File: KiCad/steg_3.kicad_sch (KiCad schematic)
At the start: 26 parts, among them U13 W65C02S

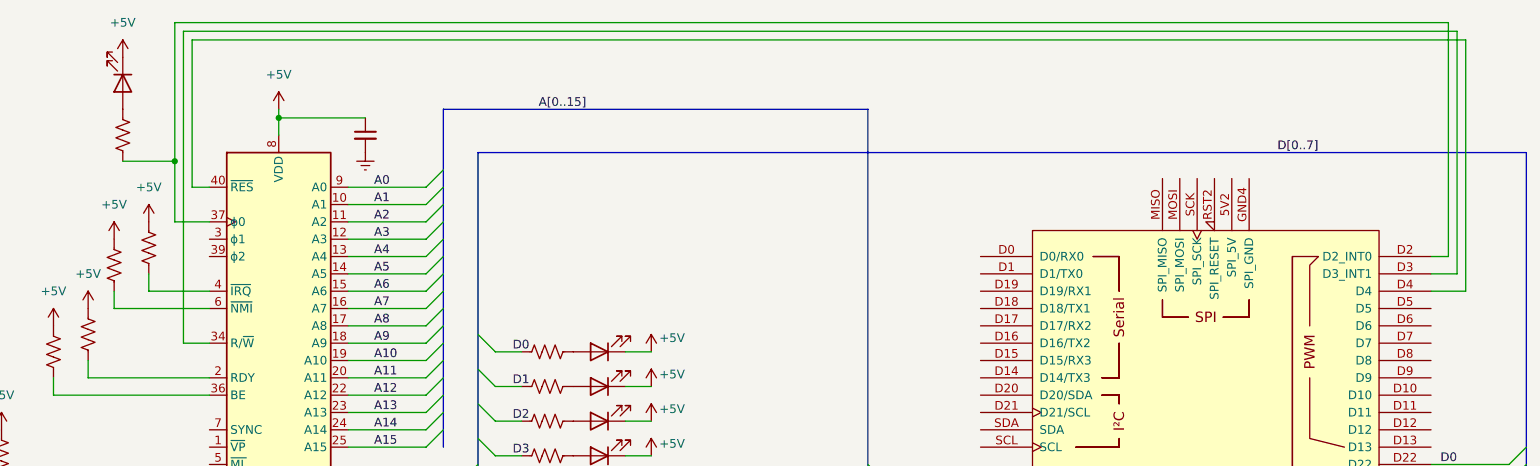
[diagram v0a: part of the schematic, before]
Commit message: Revert "Add trim potentiometer symbol and update power symbols in schematics"
This reverts commit c4bb345892a428583a00d61d4c040ffcc3a1eb40.
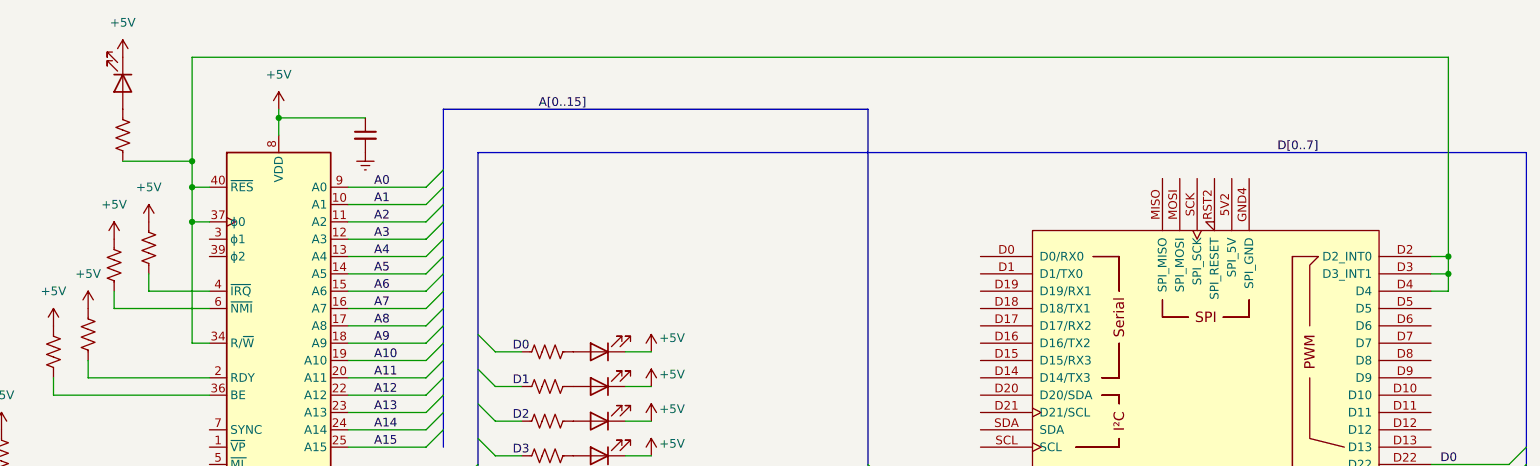
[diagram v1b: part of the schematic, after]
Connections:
- net at A7.D3 (D3_INT1), U13.34 (R/~{W}): now also A7.D2 (D2_INT0), A7.D4, R48.2, U13.37 (ϕ0), U13.40 (~{RES})
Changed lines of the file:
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@@
 	)
 	(junction
-		(at 111.76 72.39)
+		(at 298.45 86.36)
 		(diameter 0)
 		(color 0 0 0 0)
 	)
+	(junction
+		(at 114.3 81.28)
+		(diameter 0)
+		(color 0 0 0 0)
+	)
+	(junction
+		(at 298.45 88.9)
+		(diameter 0)
+		(color 0 0 0 0)
+	)
+	(junction
+		(at 114.3 72.39)
+		(diameter 0)
+		(color 0 0 0 0)
+	)
+	(junction
+		(at 114.3 76.2)
+		(diameter 0)
+		(color 0 0 0 0)
+	)
 	(bus_entry
 		(at 151.13 81.28)
@@
 	(wire
 		(pts
-			(xy 116.84 99.06) (xy 113.03 99.06)
-		)
-		(stroke
-			(width 0)
-			(type default)
-		)
-	)
-	(wire
-		(pts
-			(xy 116.84 81.28) (xy 111.76 81.28)
+			(xy 116.84 76.2) (xy 114.3 76.2)
+		)
+		(stroke
+			(width 0)
+			(type default)
+		)
+	)
+	(wire
+		(pts
+			(xy 116.84 81.28) (xy 114.3 81.28)
 		)
 		(stroke
@@
 	(wire
 		(pts
-			(xy 300.99 54.61) (xy 300.99 91.44)
-		)
-		(stroke
-			(width 0)
-			(type default)
-		)
-	)
-	(wire
-		(pts
 			(xy 137.16 127) (xy 153.67 127)
 		)
@@
 	(wire
 		(pts
-			(xy 298.45 52.07) (xy 298.45 86.36)
+			(xy 298.45 57.15) (xy 298.45 86.36)
 		)
 		(stroke
@@
 	(wire
 		(pts
+			(xy 114.3 57.15) (xy 114.3 72.39)
+		)
+		(stroke
+			(width 0)
+			(type default)
+		)
+	)
+	(wire
+		(pts
 			(xy 295.91 116.84) (xy 307.34 116.84)
 		)
@@
 	(wire
 		(pts
+			(xy 114.3 76.2) (xy 114.3 81.28)
+		)
+		(stroke
+			(width 0)
+			(type default)
+		)
+	)
+	(wire
+		(pts
+			(xy 116.84 99.06) (xy 114.3 99.06)
+		)
+		(stroke
+			(width 0)
+			(type default)
+		)
+	)
+	(wire
+		(pts
 			(xy 158.75 105.41) (xy 162.56 105.41)
 		)
@@
 	(wire
 		(pts
-			(xy 300.99 91.44) (xy 295.91 91.44)
-		)
-		(stroke
-			(width 0)
-			(type default)
-		)
-	)
-	(wire
-		(pts
 			(xy 137.16 124.46) (xy 153.67 124.46)
 		)
@@
 	(wire
 		(pts
-			(xy 111.76 52.07) (xy 298.45 52.07)
+			(xy 114.3 57.15) (xy 298.45 57.15)
+		)
+		(stroke
+			(width 0)
+			(type default)
+		)
+	)
+	(wire
+		(pts
+			(xy 295.91 91.44) (xy 298.45 91.44)
 		)
 		(stroke
@@
 	(wire
 		(pts
-			(xy 111.76 52.07) (xy 111.76 72.39)
-		)
-		(stroke
-			(width 0)
-			(type default)
-		)
-	)
-	(wire
-		(pts
-			(xy 299.72 53.34) (xy 299.72 88.9)
+			(xy 114.3 72.39) (xy 114.3 76.2)
 		)
 		(stroke
@@
 	(wire
 		(pts
-			(xy 104.14 72.39) (xy 111.76 72.39)
-		)
-		(stroke
-			(width 0)
-			(type default)
-		)
-	)
-	(wire
-		(pts
 			(xy 158.75 120.65) (xy 162.56 120.65)
 		)
@@
 	(wire
 		(pts
+			(xy 298.45 86.36) (xy 298.45 88.9)
+		)
+		(stroke
+			(width 0)
+			(type default)
+		)
+	)
+	(wire
+		(pts
 			(xy 215.9 149.86) (xy 229.87 149.86)
 		)
@@
 	(wire
 		(pts
-			(xy 111.76 72.39) (xy 111.76 81.28)
+			(xy 298.45 91.44) (xy 298.45 88.9)
 		)
 		(stroke
@@
 	(wire
 		(pts
-			(xy 116.84 76.2) (xy 114.3 76.2)
-		)
-		(stroke
-			(width 0)
-			(type default)
-		)
-	)
-	(wire
-		(pts
-			(xy 113.03 53.34) (xy 299.72 53.34)
-		)
-		(stroke
-			(width 0)
-			(type default)
-		)
-	)
-	(wire
-		(pts
 			(xy 137.16 114.3) (xy 148.59 114.3)
 		)
@@
 	(wire
 		(pts
+			(xy 104.14 72.39) (xy 114.3 72.39)
+		)
+		(stroke
+			(width 0)
+			(type default)
+		)
+	)
+	(wire
+		(pts
 			(xy 215.9 142.24) (xy 229.87 142.24)
 		)
@@
 	(wire
 		(pts
-			(xy 114.3 54.61) (xy 300.99 54.61)
-		)
-		(stroke
-			(width 0)
-			(type default)
-		)
-	)
-	(wire
-		(pts
 			(xy 116.84 93.98) (xy 102.87 93.98)
 		)
@@
 		)
 	)
-	(wire
-		(pts
-			(xy 295.91 88.9) (xy 299.72 88.9)
-		)
-		(stroke
-			(width 0)
-			(type default)
-		)
-	)
 	(bus
 		(pts
@@
 	(wire
 		(pts
+			(xy 298.45 88.9) (xy 295.91 88.9)
+		)
+		(stroke
+			(width 0)
+			(type default)
+		)
+	)
+	(wire
+		(pts
 			(xy 181.61 130.81) (xy 177.8 130.81)
 		)
@@
 	(wire
 		(pts
-			(xy 114.3 76.2) (xy 114.3 54.61)
-		)
-		(stroke
-			(width 0)
-			(type default)
-		)
-	)
-	(wire
-		(pts
 			(xy 215.9 137.16) (xy 229.87 137.16)
 		)
@@
 	(wire
 		(pts
-			(xy 113.03 99.06) (xy 113.03 53.34)
-		)
-		(stroke
+			(xy 114.3 81.28) (xy 114.3 99.06)
+		)
+		(stroke

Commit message: Add trim potentiometer symbol and update power symbols in schematics
- Introduced a new trim potentiometer symbol (Device:R_Potentiometer_Trim) with properties for reference, value, footprint, and simulation details.
- Updated existing power symbols for +5V and Earth, including new references and descriptions.
- Adjusted positions and properties of various components in the schematic to enhance clarity and organization.
- Updated multiple schematic images to reflect the latest changes.
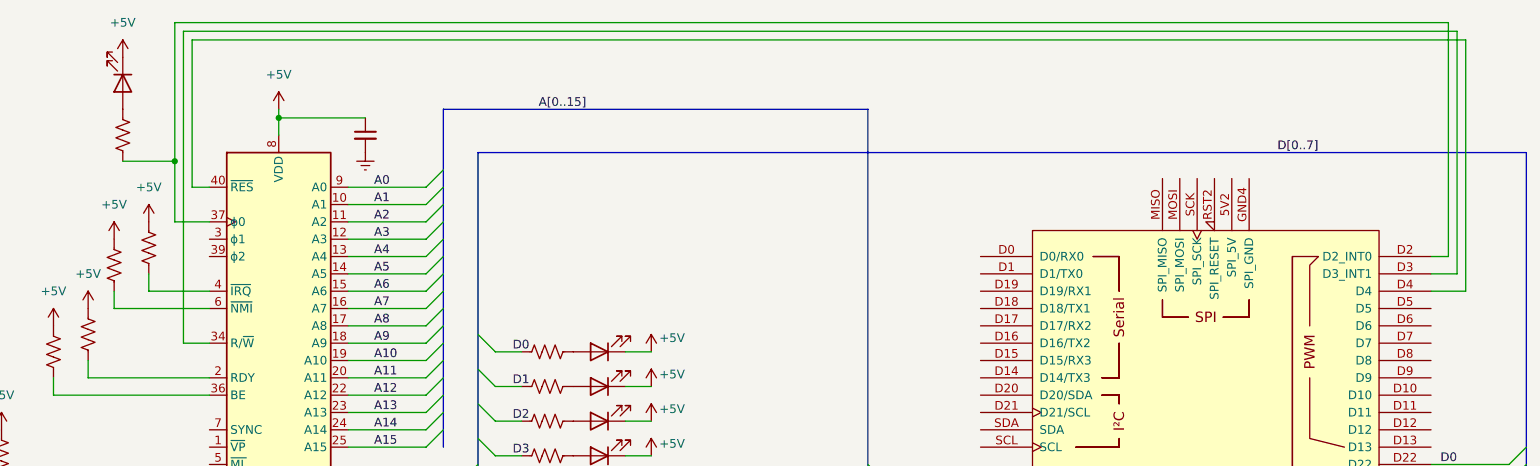
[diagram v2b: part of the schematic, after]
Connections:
- new net: A7.D3 (D3_INT1), U13.34 (R/~{W})
- new net: A7.D2 (D2_INT0), R48.2, U13.37 (ϕ0)
- new net: A7.D4, U13.40 (~{RES})
